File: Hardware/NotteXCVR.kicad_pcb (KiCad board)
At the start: 2 copper layers, 20.3 x 48.8 mm, 14 parts, among them J1 Bus_PCI_Express_x1, J2 GMI-10-2-1.27-G-10, J3 Conn_Coaxial, J4 Conn_Coaxial, J5 Conn_Coaxial, J6 Conn_Coaxial, J7 Conn_Coaxial, J8 Conn_Coaxial, U2 XC7A35T-CSG325

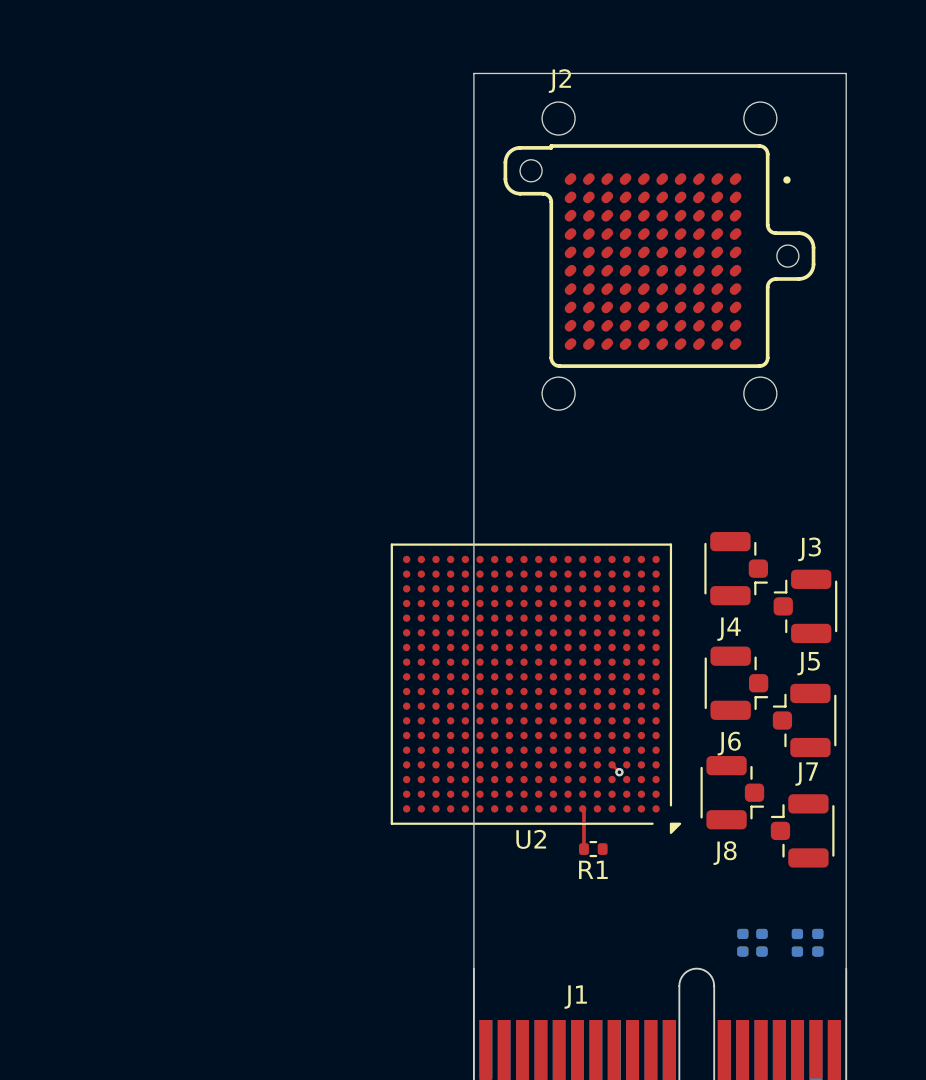
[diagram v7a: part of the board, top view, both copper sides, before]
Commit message: Made a script to fan out U2 with better precision than clicking
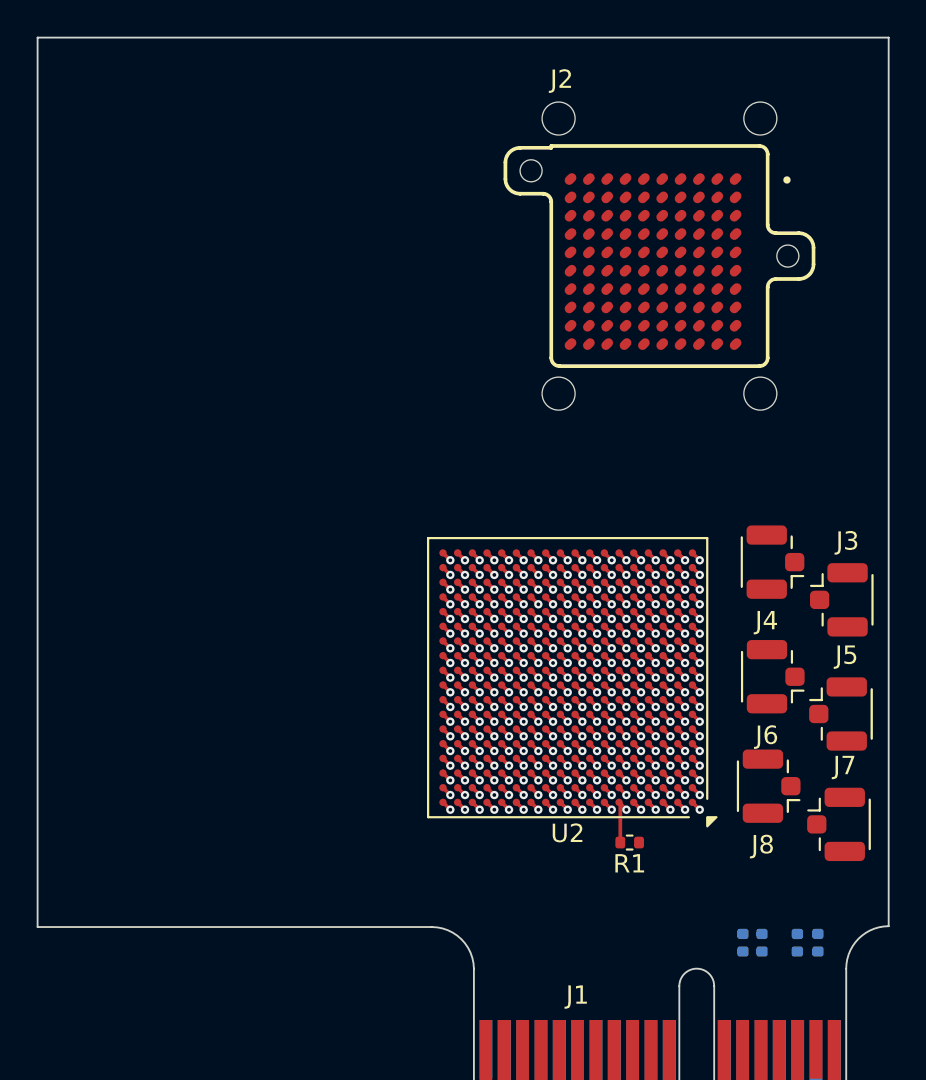
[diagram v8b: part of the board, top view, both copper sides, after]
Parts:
- moved J3 2.01 mm to (97.1, 77.7)
- moved J4 2.01 mm to (92.7, 75.6)
- moved J5 2.01 mm to (97.0, 83.9)
- moved J7 2.01 mm to (96.9, 89.9)
- moved J8 2.01 mm to (92.5, 87.8)
- moved U2 2.01 mm to (81.8, 81.9)
- moved J6 2.01 mm to (92.7, 81.9)
- moved R1 2.01 mm to (85.2, 90.9)
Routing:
- net GND: track 0.57 -> 43.0 mm, vias 1 -> 76
- net +1V0: track 0.00 -> 11.9 mm, vias 0 -> 21
- net Net-(U2A-VCCO_15-PadA16): track 0.00 -> 3.96 mm, vias 0 -> 7
- net Net-(U2A-VCCO_14-PadL16): track 0.00 -> 3.96 mm, vias 0 -> 7
- net +1V8: track 0.00 -> 3.96 mm, vias 0 -> 7
- net Net-(U2B-VCCO_34-PadL6): track 0.00 -> 3.39 mm, vias 0 -> 6
- net MGTAVTT: track 0.00 -> 2.83 mm, vias 0 -> 5
- net MGTAVCC: track 0.00 -> 2.26 mm, vias 0 -> 4
- net unconnected-(U2E-VREFN_0-PadK9): track 0.00 -> 0.57 mm, vias 0 -> 1
- net unconnected-(U2E-VP_0-PadK10): track 0.00 -> 0.57 mm, vias 0 -> 1
- net unconnected-(U2E-VCCO_0-PadR10): track 0.00 -> 0.57 mm, vias 0 -> 1
- net unconnected-(U2E-VCCO_0-PadE10): track 0.00 -> 0.57 mm, vias 0 -> 1
- net unconnected-(U2E-PROGRAM_B_0-PadP10): track 0.00 -> 0.57 mm, vias 0 -> 1
- net unconnected-(U2E-M1_0-PadR11): track 0.00 -> 0.57 mm, vias 0 -> 1
- net unconnected-(U2B-IO_L9P_T1_DQS_34-PadN1): track 0.00 -> 0.57 mm, vias 0 -> 1
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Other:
- board size 20.3 x 48.8 mm -> 46.4 x 50.8 mm
